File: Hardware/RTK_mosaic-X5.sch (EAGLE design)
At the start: 235 parts, among them J2 MAGJACK-POE, J3 MICRO-SD-PUSH-PUSH-EXT-PIN, J4 Vertical Qwiic Connector, J9 MAGJACK-POE, U1 ESP32-WROVER-IE, U10 POE_PSU-DP990X, U11 SN74AVC4T774PW, U17 URB2405YMD, U2 CH340C, U3 XC6222B331MR-G, U4 TXS0108, U5 TXS0108, U6 XC6222B331MR-G, U7 KSZ8041NL, U8 MOSAIC-X5X5, U9 KSZ8041NL

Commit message: Tweaked and panelized
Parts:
- removed ACT, ACT2: JUMPER-SMT_2_NC_TRACE_SILK, SparkFun-Jumpers:JUMPER-SMT_2_NC_TRACE_SILK
- added SPEED, SPEED2: JUMPER-SMT_2_NC_TRACE_SILK, SparkFun-Jumpers:JUMPER-SMT_2_NC_TRACE_SILK
- FRAME3: DESIGNER Paul Clark -> (none); REV V01 -> (none)
- U3, U6: value XC6222B331MR-G -> AP7361C-33FGEUDFN-8; device SparkFun-IC-Power:XC6222B331MR-G -> SparkFun-IC-Power:AP7361C-33FGEUDFN-8
- U8: device Septentrio_Mosaic:MOSAIC-X5X5 -> Septentrio_mosaic-X5:MOSAIC-X5X5
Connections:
- net ACT_ESP32 renamed SPEED_ESP32
- net ACT_MOSAIC renamed SPEED_MOSAIC
- net N$13 renamed ESP32_RF
- removed net ACT: ACT.1, J9.GRN-
- removed net ACT2: ACT2.1, J2.GRN-
- removed net LINK: J9.YLW-, LINK.1
- removed net LINK2: J2.YLW-, LINK2.1
- new net N$3: J9.GRN-, LINK.1
- new net N$40: J2.GRN-, LINK2.1
- new net N$41: J2.YLW-, SPEED2.1
- new net N$7: J9.YLW-, SPEED.1
- net N$12: now also SPEED.2; no longer ACT.2
- net N$142: now also SPEED2.2; no longer ACT2.2
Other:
- note added: "AP7361C-33 Vin Max: 6.0V Iout Max: 1A (Limit 1.5A Typ) Vdo: 360mV @ 1A Output Discharge: 100Ω Typ"
- note added: "Vin Max: 6.0V Iout Max: 1A (Limit 1.5A Typ) Vdo: 360mV @ 1A Output Discharge: 100Ω Typ"
- note removed: "Vin Max: 6.0V Iout Max: 700mA Vdo: 120mV @ 330mA Output Discharge: 530Ω Typ"
- moved on the sheet: BT, C10, C14, C15, C6, C7, C8, C9, D11, D12, D13, D15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

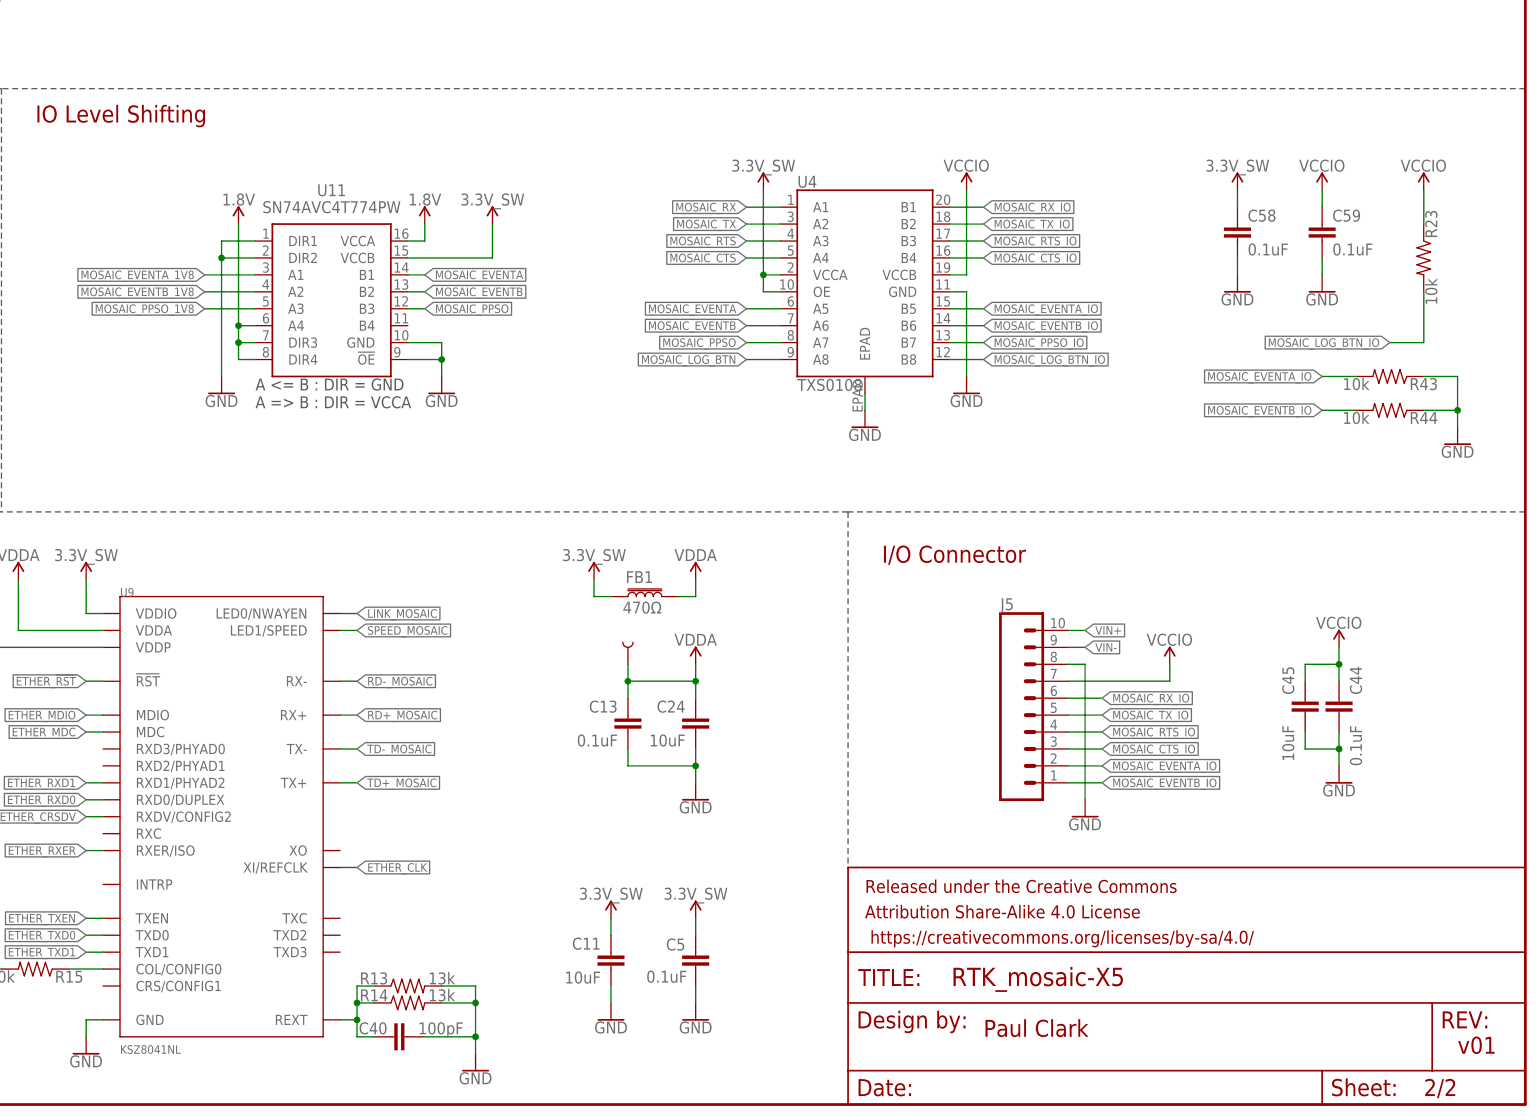
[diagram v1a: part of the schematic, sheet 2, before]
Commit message: Correct Ethernet PHY pad numbering. Needs re-panelizing
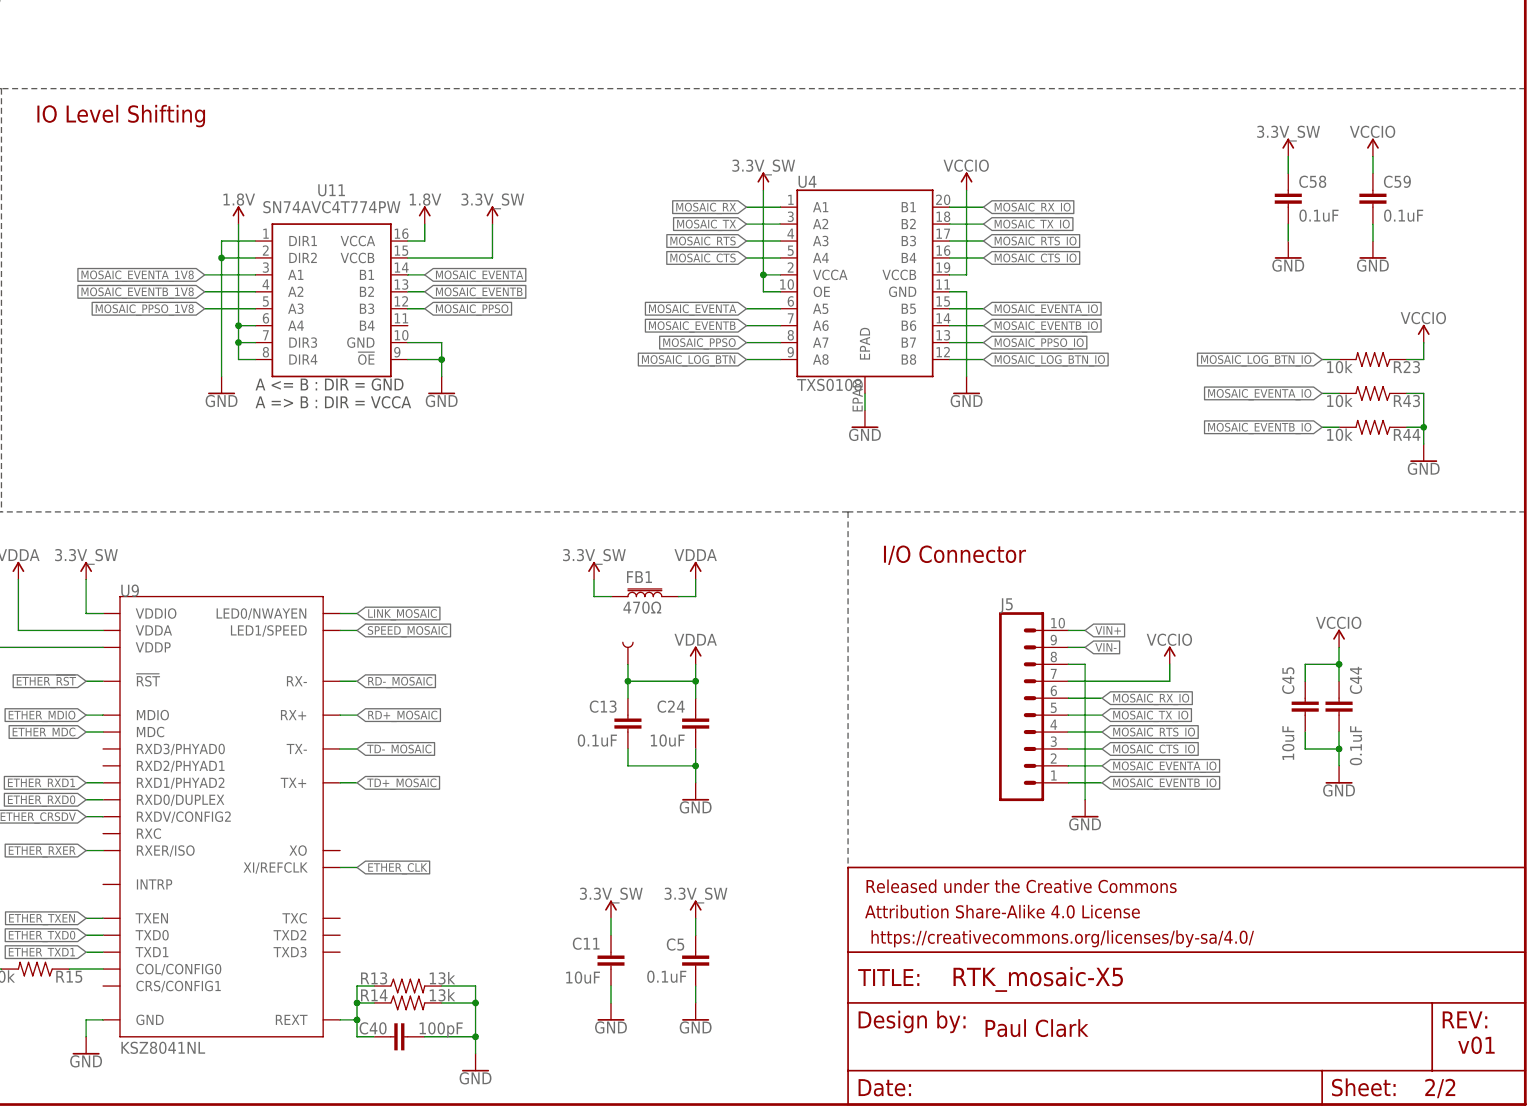
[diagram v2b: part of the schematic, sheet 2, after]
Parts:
- U7, U9: device Septentrio_Mosaic:KSZ8041NL -> Septentrio_mosaic-X5:KSZ8041NL
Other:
- moved on the sheet: C58, C59, R23, R43, R44

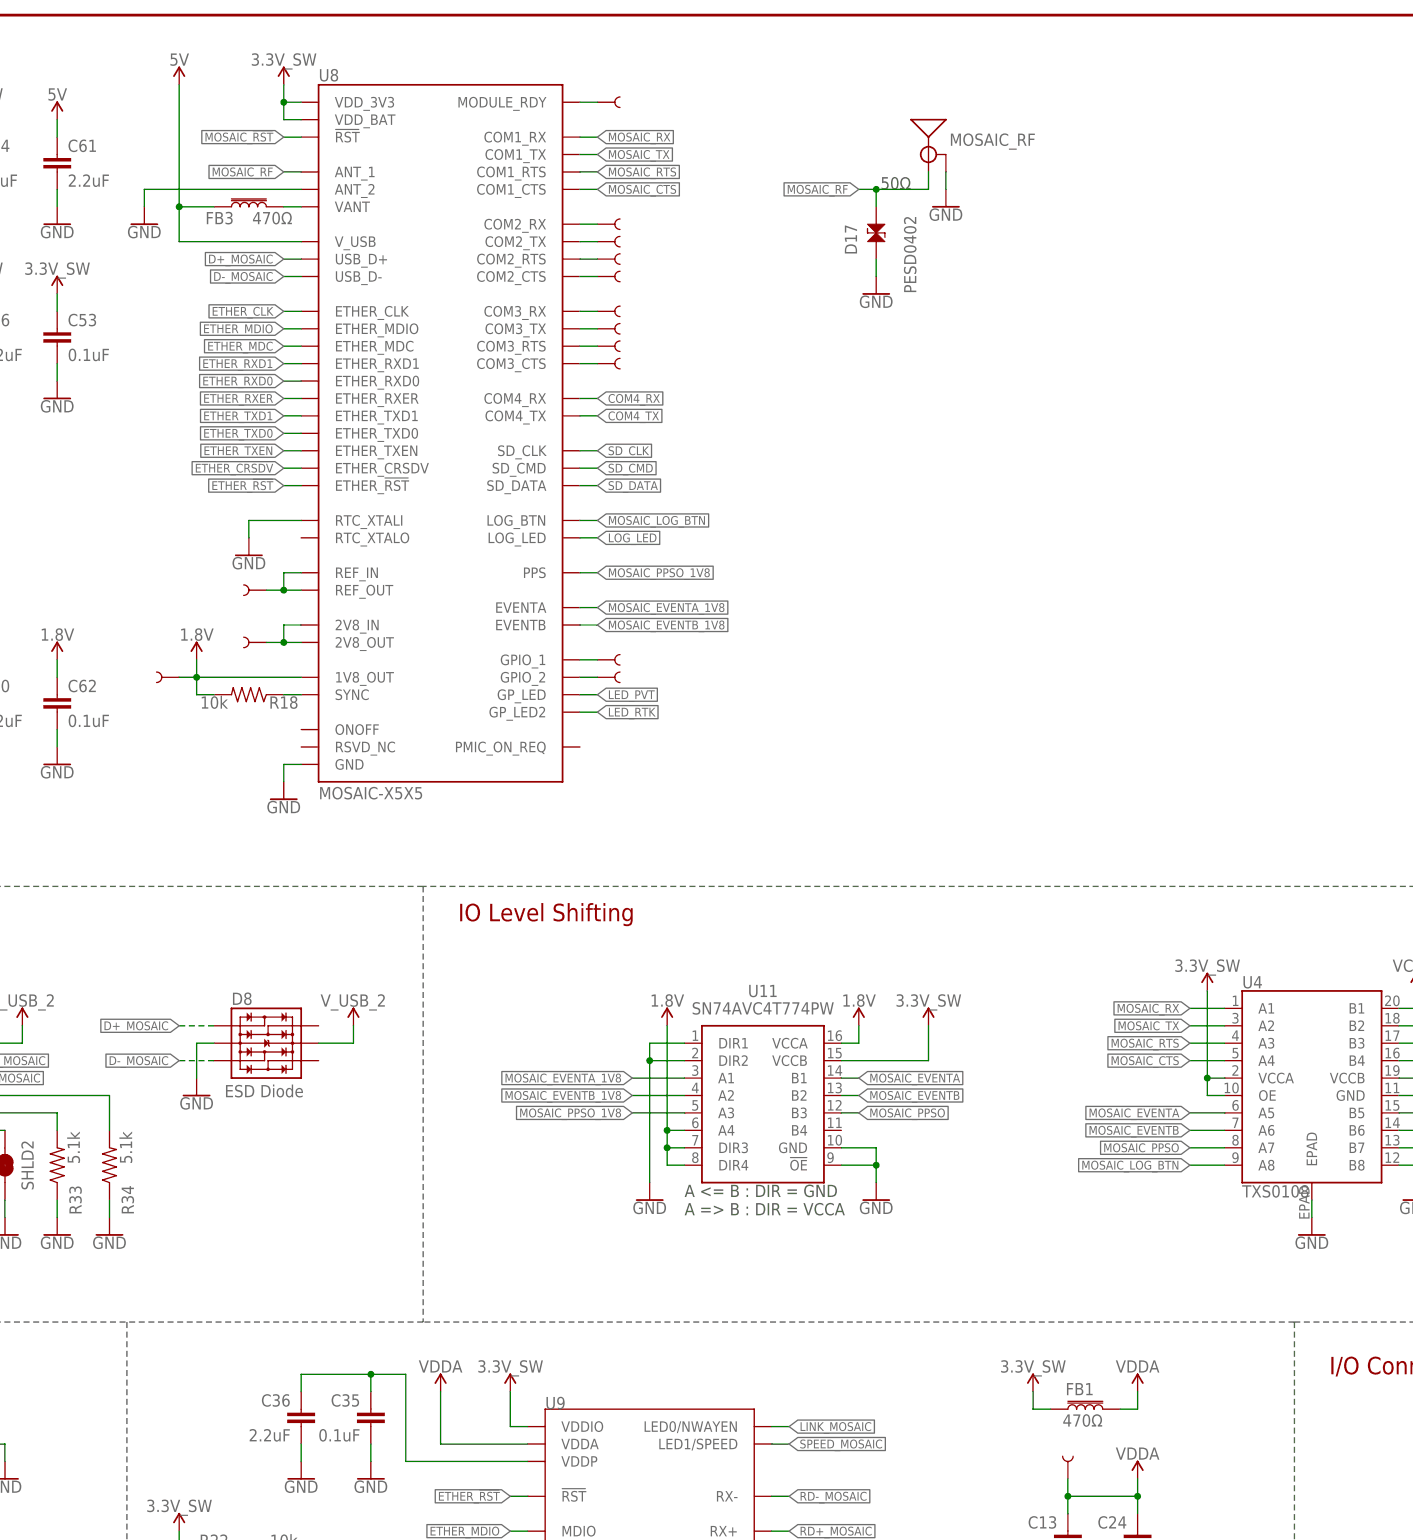
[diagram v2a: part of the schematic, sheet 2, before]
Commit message: Add second antenna connector for future mosaic-H product
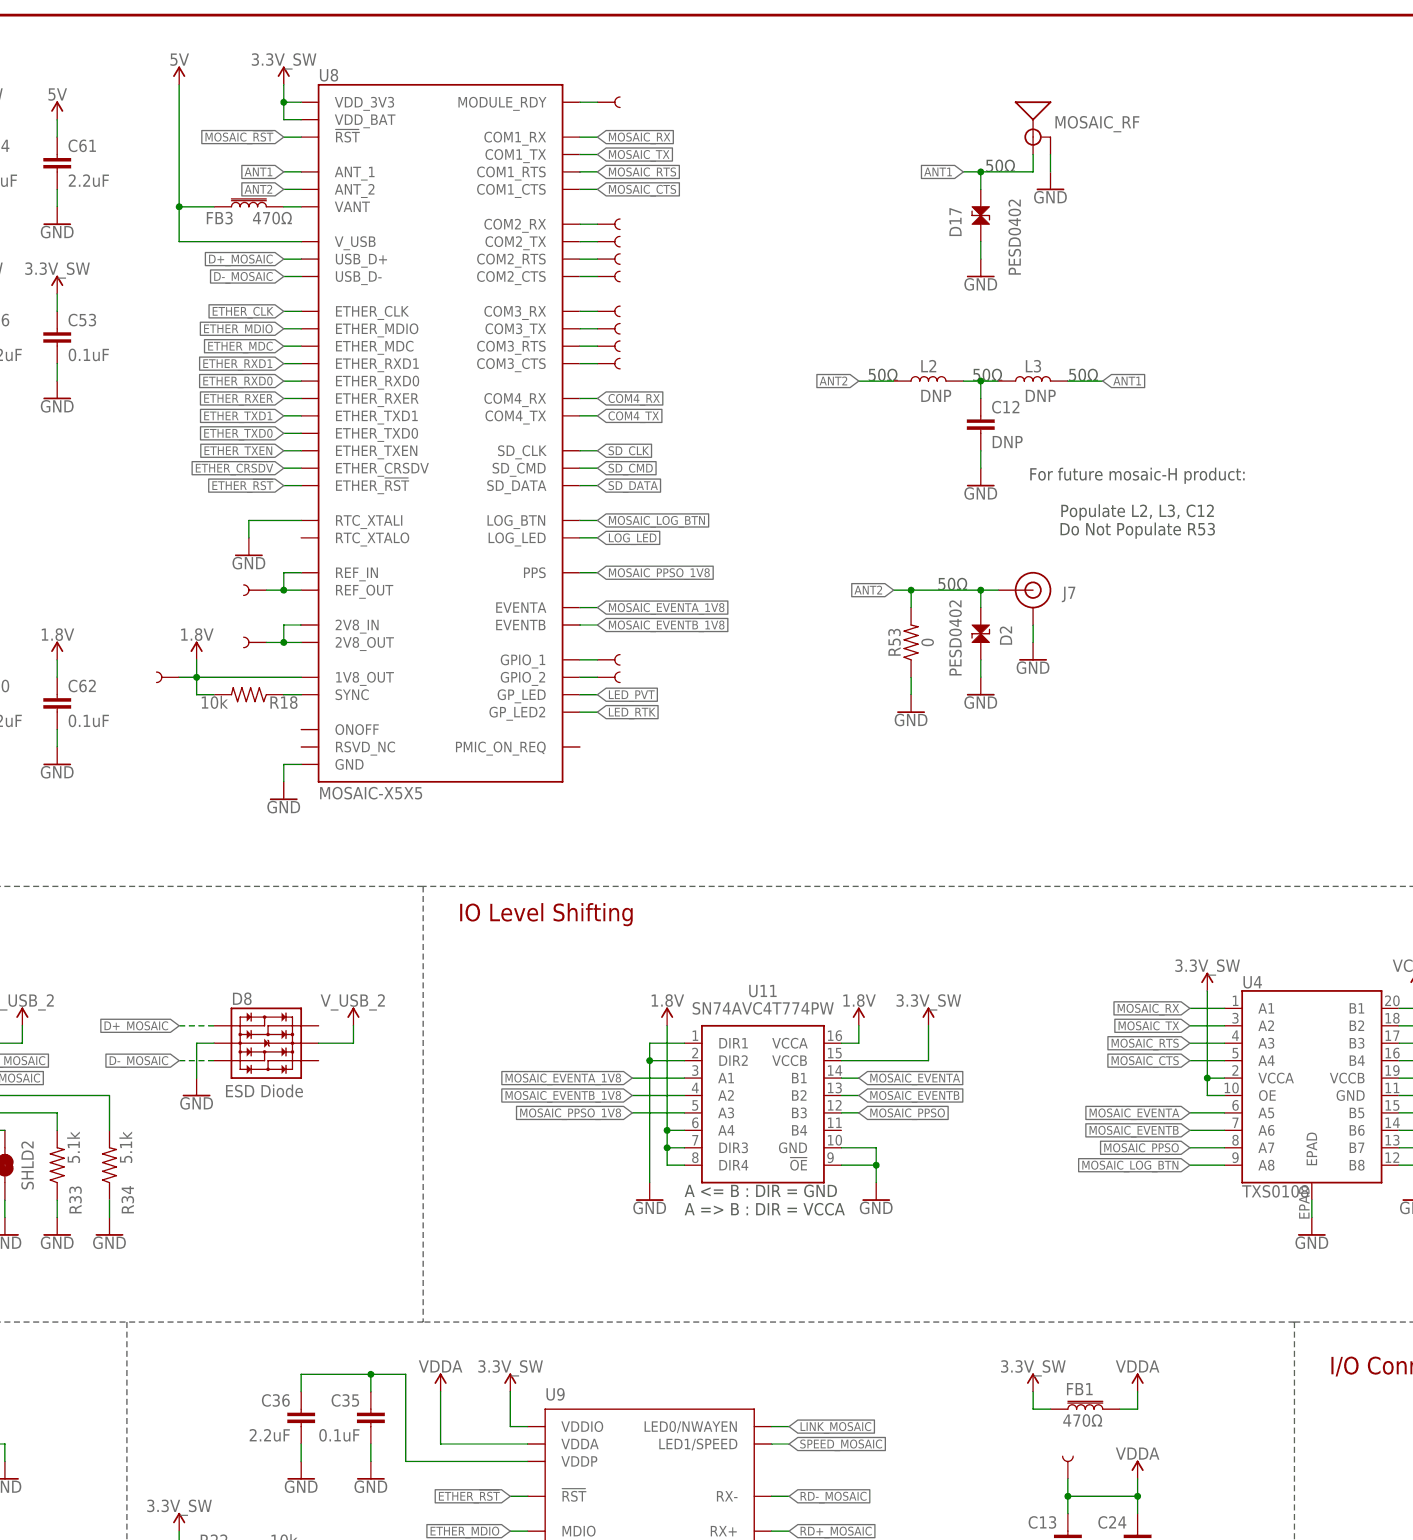
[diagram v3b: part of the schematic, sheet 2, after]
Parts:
- added C12: DNP, SparkFun-Capacitors:DNP-0603_NO_CREAM
- added D2: PESD0402, SparkFun-DiscreteSemi:PESD0402-0402
- added H10, H7, H8: STAND-OFFTIGHT, SparkFun-Hardware:STAND-OFFTIGHT
- added J7: (no value), SparkFun-Connectors:U.FL2PIN-REDUCED-FOOTPRINT
- added L2, L3: DNP, SparkFun-Coils:DNP-0603_NO-CREAM
- added R53: 0, SparkFun-Resistors:0OHM-0603-1/10W
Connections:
- removed net MOSAIC_RF: D17.1, MOSAIC_RF.SIGNAL, U8.ANT_1
- new net ANT1: D17.1, L3.2, MOSAIC_RF.SIGNAL, U8.ANT_1
- new net ANT2: D2.1, J7.SIGNAL, L2.1, R53.2, U8.ANT_2
- new net N$13: C12.1, L2.2, L3.1
- net GND: now also C12.2, D2.2, J7.GND, R53.1; no longer U8.ANT_2
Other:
- note added: "For future mosaic-H product: Populate L2, L3, C12 Do Not Populate R53"
- moved on the sheet: D17, MOSAIC_RF
